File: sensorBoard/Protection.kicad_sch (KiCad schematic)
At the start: 7 parts

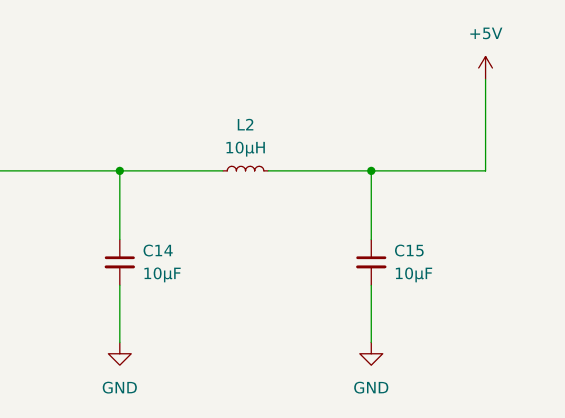
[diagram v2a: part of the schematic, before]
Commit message: started to connect layout. added 0 Ohm resistors to separate the drivers.
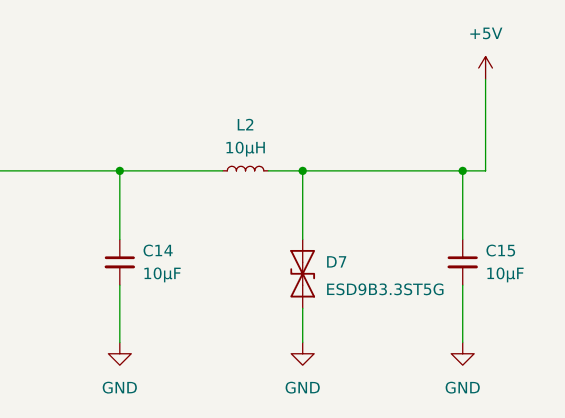
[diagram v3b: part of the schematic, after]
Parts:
- added D7: ESD9B3.3ST5G, Diode_SMD:D_SOD-523, symbol Diode:ESD9B3.3ST5G
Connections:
- net +5V: now also D7.2 (A2)
- net GND: now also D7.1 (A1)
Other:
- moved on the sheet: C15
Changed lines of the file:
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@@
 	)
 	(junction
-		(at 121.92 101.6)
+		(at 114.3 101.6)
+		(diameter 0)
+		(color 0 0 0 0)
+	)
+	(junction
+		(at 132.08 101.6)
 		(diameter 0)
 		(color 0 0 0 0)
@@
 	(wire
 		(pts
-			(xy 121.92 101.6) (xy 134.62 101.6)
-		)
-		(stroke
-			(width 0)
-			(type default)
-		)
-	)
-	(wire
-		(pts
 			(xy 106.68 59.69) (xy 106.68 63.5)
 		)
@@
 	(wire
 		(pts
-			(xy 110.49 101.6) (xy 121.92 101.6)
+			(xy 110.49 101.6) (xy 114.3 101.6)
 		)
 		(stroke
@@
 	(wire
 		(pts
-			(xy 121.92 101.6) (xy 121.92 109.22)
+			(xy 114.3 101.6) (xy 132.08 101.6)
+		)
+		(stroke
+			(width 0)
+			(type default)
+		)
+	)
+	(wire
+		(pts
+			(xy 132.08 101.6) (xy 132.08 109.22)
 		)
 		(stroke
@@
 	(wire
 		(pts
-			(xy 121.92 114.3) (xy 121.92 120.65)
+			(xy 132.08 101.6) (xy 134.62 101.6)
+		)
+		(stroke
+			(width 0)
+			(type default)
+		)
+	)
+	(wire
+		(pts
+			(xy 114.3 116.84) (xy 114.3 120.65)
+		)
+		(stroke
+			(width 0)
+			(type default)
+		)
+	)
+	(wire
+		(pts
+			(xy 132.08 114.3) (xy 132.08 120.65)
 		)
 		(stroke
@@
 		(pts
 			(xy 106.68 50.8) (xy 106.68 52.07)
+		)
+		(stroke
+			(width 0)
+			(type default)
+		)
+	)
+	(wire
+		(pts
+			(xy 114.3 101.6) (xy 114.3 109.22)
 		)
 		(stroke
@@
 	(symbol
 		(lib_id "power:GND")
-		(at 121.92 120.65 0)
+		(at 132.08 120.65 0)
 		(unit 1)
 		(exclude_from_sim no)
@@
 		(fields_autoplaced yes)
 		(property "Reference" "#PWR049"
-			(at 121.92 127 0)
+			(at 132.08 127 0)
 			(effects
 				(font
@@
 		)
 		(property "Value" "GND"
-			(at 121.92 125.73 0)
+			(at 132.08 125.73 0)
 			(effects
 				(font
@@
 		)
 		(property "Footprint" ""
-			(at 121.92 120.65 0)
+			(at 132.08 120.65 0)
 			(effects
 				(font
@@
 		)
 		(property "Datasheet" ""
-			(at 121.92 120.65 0)
+			(at 132.08 120.65 0)
 			(effects
 				(font
@@
 		)
 		(property "Description" "Power symbol creates a global label with name \"GND\" , ground"
-			(at 121.92 120.65 0)
+			(at 132.08 120.65 0)
 			(effects
 				(font
@@
 	(symbol
 		(lib_id "Device:C_Small")
-		(at 121.92 111.76 0)
+		(at 132.08 111.76 0)
 		(unit 1)
 		(exclude_from_sim no)
@@
 		(fields_autoplaced yes)
 		(property "Reference" "C15"
-			(at 124.46 110.4962 0)
+			(at 134.62 110.4962 0)
 			(effects
 				(font
@@
 		)
 		(property "Value" "10µF"
-			(at 124.46 113.0362 0)
+			(at 134.62 113.0362 0)
 			(effects
 				(font
@@
 		)
 		(property "Footprint" "Capacitor_SMD:C_1210_3225Metric"
-			(at 121.92 111.76 0)
+			(at 132.08 111.76 0)
 			(effects
 				(font
@@
 		)
 		(property "Datasheet" "~"
-			(at 121.92 111.76 0)
+			(at 132.08 111.76 0)
 			(effects
 				(font
@@
 		)
 		(property "Description" "Unpolarized capacitor, small symbol"
-			(at 121.92 111.76 0)
+			(at 132.08 111.76 0)
 			(effects
 				(font
@@
 	)
 	(symbol
+		(lib_id "Diode:ESD9B3.3ST5G")
+		(at 114.3 113.03 90)
+		(unit 1)
+		(exclude_from_sim no)
+		(in_bom yes)
+		(on_board yes)
+		(dnp no)
+		(property "Reference" "D7"
+			(at 116.84 111.7599 90)
+			(effects
+				(font
+					(size 1.27 1.27)
+				)
+				(justify right)
+			)
+		)
+		(property "Value" "ESD9B3.3ST5G"
+			(at 116.84 114.808 90)
+			(effects
+				(font
+					(size 1.27 1.27)
+				)
+				(justify right)
+			)
+		)
+		(property "Footprint" "Diode_SMD:D_SOD-523"
+			(at 114.3 113.03 0)
+			(effects
+				(font
+					(size 1.27 1.27)
+				)
+				(hide yes)
+			)
+		)
+		(property "Datasheet" "https://www.mouser.de/ProductDetail/Littelfuse/SMBJ13A?qs=HR2RnyOI4E7jYyaNBU0w0w%3D%3D&srsltid=AfmBOor6_agX3vir1GVOfC2EUzzLngFgs9YFDGWrTlkz9UynbndBGqlu"
+			(at 114.3 113.03 0)
+			(effects
+				(font
+					(size 1.27 1.27)
+				)
+				(hide yes)
+			)
+		)
+		(property "Description" "ESD protection diode, 3.3Vrwm, SOD-923"
+			(at 114.3 113.03 0)
+			(effects
+				(font
+					(size 1.27 1.27)
+				)
+				(hide yes)
+			)
+		)
+		(pin "1"
+		)
+		(pin "2"
+		)
+		(instances
+			(project "sensorBoard"
+				(path "/df1584e9-54f0-49dc-b423-5f64048efa01/eeb71e0f-46bb-44dd-988f-3e7d2427e332"
+					(reference "D7")
+					(unit 1)
+				)
+			)
+		)
+	)
+	(symbol
 		(lib_id "power:GND")
 		(at 127 63.5 0)
@@
 					(unit 1)
 				)
+			)
+		)
+	)
+	(symbol
+		(lib_id "power:GND")
+		(at 114.3 120.65 0)
+		(unit 1)
+		(exclude_from_sim no)
+		(in_bom yes)
+		(on_board yes)
+		(dnp no)
+		(fields_autoplaced yes)
+		(property "Reference" "#PWR083"
+			(at 114.3 127 0)
+			(effects
+				(font
+					(size 1.27 1.27)
+				)
+				(hide yes)
+			)
+		)
+		(property "Value" "GND"
+			(at 114.3 125.73 0)
+			(effects
+				(font
+					(size 1.27 1.27)
+				)
+			)
+		)
+		(property "Footprint" ""
+			(at 114.3 120.65 0)
+			(effects
+				(font
+					(size 1.27 1.27)
+				)
+				(hide yes)
+			)
+		)
+		(property "Datasheet" ""
+			(at 114.3 120.65 0)
+			(effects
+				(font
+					(size 1.27 1.27)
+				)
+				(hide yes)
+			)
+		)
+		(property "Description" "Power symbol creates a global label with name \"GND\" , ground"
+			(at 114.3 120.65 0)
+			(effects
+				(font
+					(size 1.27 1.27)
+				)
+				(hide yes)
+			)
+		)
+		(pin "1"
+		)
+		(instances
+			(project "sensorBoard"
+				(path "/df1584e9-54f0-49dc-b423-5f64048efa01/eeb71e0f-46bb-44dd-988f-3e7d2427e332"
+					(reference "#PWR083")
+					(unit 1)
+				)

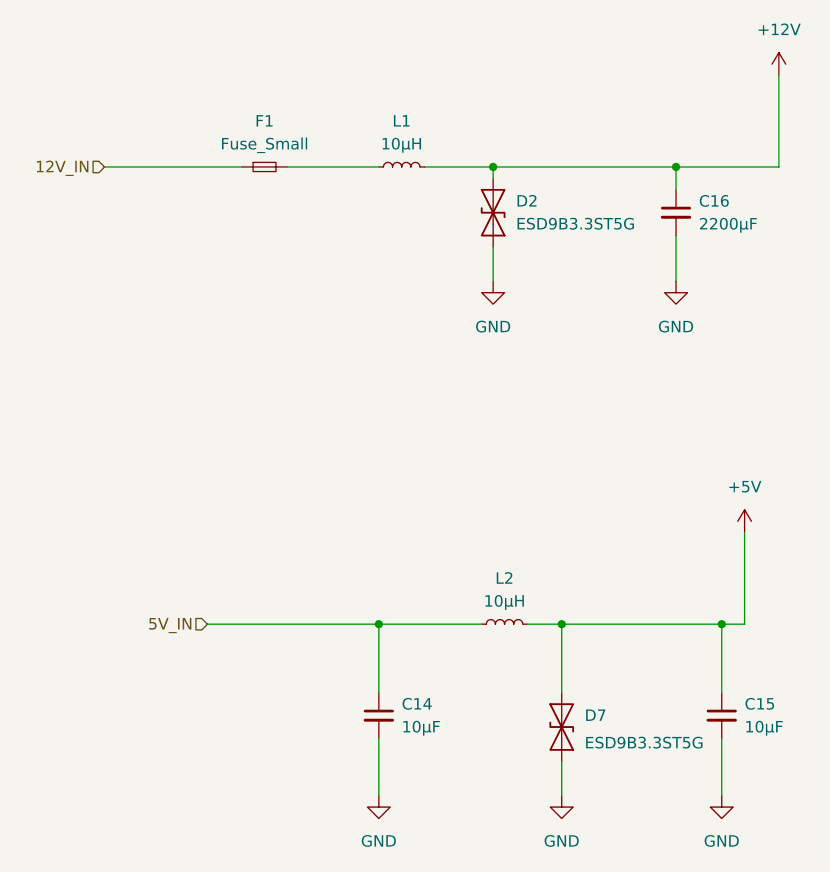
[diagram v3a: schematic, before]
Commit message: new two separate pcbs
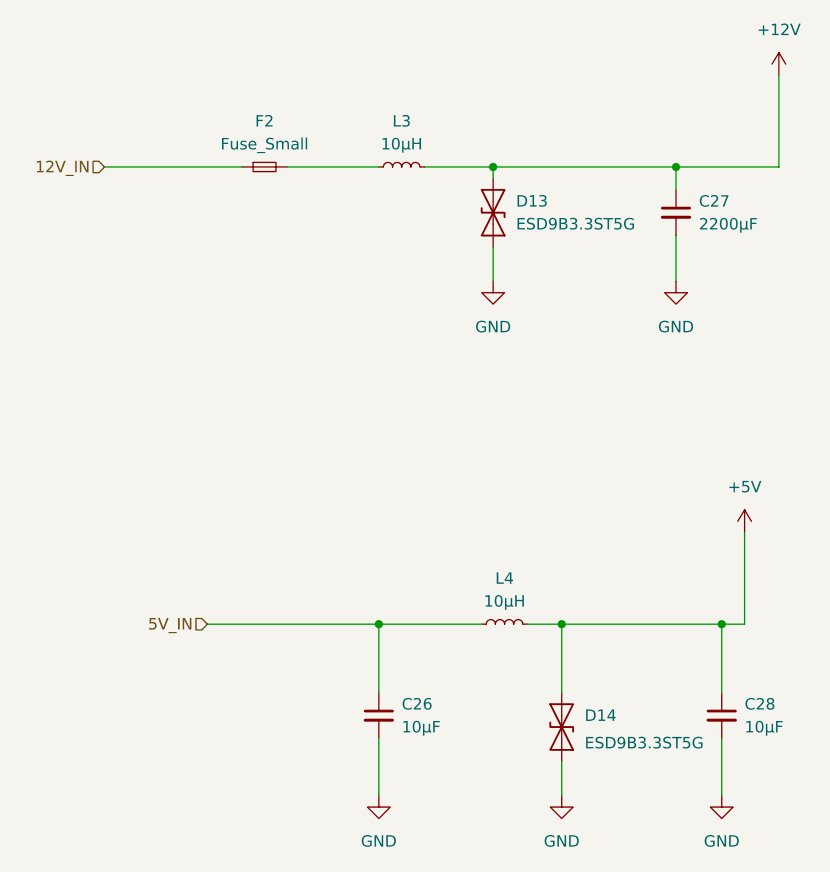
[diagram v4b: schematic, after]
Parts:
- renumbered C14 to C26, C16 to C27, C15 to C28, D2 to D13, D7 to D14, F1 to F2, L1 to L3, L2 to L4
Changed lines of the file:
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@@
 		(dnp no)
 		(fields_autoplaced yes)
-		(property "Reference" "L2"
+		(property "Reference" "L4"
 			(at 107.95 96.52 90)
 			(effects
@@
 		(instances
 			(project "sensorBoard"
-				(path "/df1584e9-54f0-49dc-b423-5f64048efa01/eeb71e0f-46bb-44dd-988f-3e7d2427e332"
-					(reference "L2")
+				(path "/df1584e9-54f0-49dc-b423-5f64048efa01/60fa4213-9bcb-42a7-994a-420953d9bcb7/85dfac51-e25c-4ad4-a068-3d93efddec4c"
+					(reference "L6")
+					(unit 1)
+				)
+				(path "/df1584e9-54f0-49dc-b423-5f64048efa01/99847452-c15f-478e-a49b-00c0f2bcd04b/3442ede8-ab67-47a2-877b-54a427eb9a90"
+					(reference "L4")
 					(unit 1)
 				)
@@
 		(dnp no)
 		(fields_autoplaced yes)
-		(property "Reference" "#PWR049"
+		(property "Reference" "#PWR0128"
 			(at 132.08 127 0)
 			(effects
@@
 		(instances
 			(project "sensorBoard"
-				(path "/df1584e9-54f0-49dc-b423-5f64048efa01/eeb71e0f-46bb-44dd-988f-3e7d2427e332"
-					(reference "#PWR049")
+				(path "/df1584e9-54f0-49dc-b423-5f64048efa01/60fa4213-9bcb-42a7-994a-420953d9bcb7/85dfac51-e25c-4ad4-a068-3d93efddec4c"
+					(reference "#PWR0210")
+					(unit 1)
+				)
+				(path "/df1584e9-54f0-49dc-b423-5f64048efa01/99847452-c15f-478e-a49b-00c0f2bcd04b/3442ede8-ab67-47a2-877b-54a427eb9a90"
+					(reference "#PWR0128")
 					(unit 1)
 				)
@@
 		(dnp no)
 		(fields_autoplaced yes)
-		(property "Reference" "C15"
+		(property "Reference" "C28"
 			(at 134.62 110.4962 0)
 			(effects
@@
 		(instances
 			(project "sensorBoard"
-				(path "/df1584e9-54f0-49dc-b423-5f64048efa01/eeb71e0f-46bb-44dd-988f-3e7d2427e332"
-					(reference "C15")
+				(path "/df1584e9-54f0-49dc-b423-5f64048efa01/60fa4213-9bcb-42a7-994a-420953d9bcb7/85dfac51-e25c-4ad4-a068-3d93efddec4c"
+					(reference "C45")
+					(unit 1)
+				)
+				(path "/df1584e9-54f0-49dc-b423-5f64048efa01/99847452-c15f-478e-a49b-00c0f2bcd04b/3442ede8-ab67-47a2-877b-54a427eb9a90"
+					(reference "C28")
 					(unit 1)
 				)
@@
 		(dnp no)
 		(fields_autoplaced yes)
-		(property "Reference" "#PWR045"
+		(property "Reference" "#PWR0130"
 			(at 138.43 44.45 0)
 			(effects
@@
 		)
 		(instances
-			(project ""
-				(path "/df1584e9-54f0-49dc-b423-5f64048efa01/eeb71e0f-46bb-44dd-988f-3e7d2427e332"
-					(reference "#PWR045")
+			(project "sensorBoard"
+				(path "/df1584e9-54f0-49dc-b423-5f64048efa01/60fa4213-9bcb-42a7-994a-420953d9bcb7/85dfac51-e25c-4ad4-a068-3d93efddec4c"
+					(reference "#PWR0212")
+					(unit 1)
+				)
+				(path "/df1584e9-54f0-49dc-b423-5f64048efa01/99847452-c15f-478e-a49b-00c0f2bcd04b/3442ede8-ab67-47a2-877b-54a427eb9a90"
+					(reference "#PWR0130")
 					(unit 1)
 				)
@@
 		(on_board yes)
 		(dnp no)
-		(property "Reference" "D7"
+		(property "Reference" "D14"
 			(at 116.84 111.7599 90)
 			(effects
@@
 		(instances
 			(project "sensorBoard"
-				(path "/df1584e9-54f0-49dc-b423-5f64048efa01/eeb71e0f-46bb-44dd-988f-3e7d2427e332"
-					(reference "D7")
+				(path "/df1584e9-54f0-49dc-b423-5f64048efa01/60fa4213-9bcb-42a7-994a-420953d9bcb7/85dfac51-e25c-4ad4-a068-3d93efddec4c"
+					(reference "D21")
+					(unit 1)
+				)
+				(path "/df1584e9-54f0-49dc-b423-5f64048efa01/99847452-c15f-478e-a49b-00c0f2bcd04b/3442ede8-ab67-47a2-877b-54a427eb9a90"
+					(reference "D14")
 					(unit 1)
 				)
@@
 		(dnp no)
 		(fields_autoplaced yes)
-		(property "Reference" "#PWR050"
+		(property "Reference" "#PWR0127"
 			(at 127 69.85 0)
 			(effects
@@
 		)
 		(instances
-			(project ""
-				(path "/df1584e9-54f0-49dc-b423-5f64048efa01/eeb71e0f-46bb-44dd-988f-3e7d2427e332"
-					(reference "#PWR050")
+			(project "sensorBoard"
+				(path "/df1584e9-54f0-49dc-b423-5f64048efa01/60fa4213-9bcb-42a7-994a-420953d9bcb7/85dfac51-e25c-4ad4-a068-3d93efddec4c"
+					(reference "#PWR0209")
+					(unit 1)
+				)
+				(path "/df1584e9-54f0-49dc-b423-5f64048efa01/99847452-c15f-478e-a49b-00c0f2bcd04b/3442ede8-ab67-47a2-877b-54a427eb9a90"
+					(reference "#PWR0127")
 					(unit 1)
 				)
@@
 		(dnp no)
 		(fields_autoplaced yes)
-		(property "Reference" "L1"
+		(property "Reference" "L3"
 			(at 96.52 45.72 90)
 			(effects
@@
 		)
 		(instances
-			(project ""
-				(path "/df1584e9-54f0-49dc-b423-5f64048efa01/eeb71e0f-46bb-44dd-988f-3e7d2427e332"
-					(reference "L1")
+			(project "sensorBoard"
+				(path "/df1584e9-54f0-49dc-b423-5f64048efa01/60fa4213-9bcb-42a7-994a-420953d9bcb7/85dfac51-e25c-4ad4-a068-3d93efddec4c"
+					(reference "L5")
+					(unit 1)
+				)
+				(path "/df1584e9-54f0-49dc-b423-5f64048efa01/99847452-c15f-478e-a49b-00c0f2bcd04b/3442ede8-ab67-47a2-877b-54a427eb9a90"
+					(reference "L3")
 					(unit 1)
 				)
@@
 		(dnp no)
 		(fields_autoplaced yes)
-		(property "Reference" "#PWR048"
+		(property "Reference" "#PWR0124"
 			(at 93.98 127 0)
 			(effects
@@
 		)
 		(instances
-			(project ""
-				(path "/df1584e9-54f0-49dc-b423-5f64048efa01/eeb71e0f-46bb-44dd-988f-3e7d2427e332"
-					(reference "#PWR048")
+			(project "sensorBoard"
+				(path "/df1584e9-54f0-49dc-b423-5f64048efa01/60fa4213-9bcb-42a7-994a-420953d9bcb7/85dfac51-e25c-4ad4-a068-3d93efddec4c"
+					(reference "#PWR0206")
+					(unit 1)
+				)
+				(path "/df1584e9-54f0-49dc-b423-5f64048efa01/99847452-c15f-478e-a49b-00c0f2bcd04b/3442ede8-ab67-47a2-877b-54a427eb9a90"
+					(reference "#PWR0124")
 					(unit 1)
 				)
@@
 		(dnp no)
 		(fields_autoplaced yes)
-		(property "Reference" "D2"
+		(property "Reference" "D13"
 			(at 109.22 54.6099 90)
 			(effects
@@
 		)
 		(instances
-			(project ""
-				(path "/df1584e9-54f0-49dc-b423-5f64048efa01/eeb71e0f-46bb-44dd-988f-3e7d2427e332"
-					(reference "D2")
+			(project "sensorBoard"
+				(path "/df1584e9-54f0-49dc-b423-5f64048efa01/60fa4213-9bcb-42a7-994a-420953d9bcb7/85dfac51-e25c-4ad4-a068-3d93efddec4c"
+					(reference "D20")
+					(unit 1)
+				)
+				(path "/df1584e9-54f0-49dc-b423-5f64048efa01/99847452-c15f-478e-a49b-00c0f2bcd04b/3442ede8-ab67-47a2-877b-54a427eb9a90"
+					(reference "D13")
 					(unit 1)
 				)
@@
 		(dnp no)
 		(fields_autoplaced yes)
-		(property "Reference" "#PWR083"
+		(property "Reference" "#PWR0126"
 			(at 114.3 127 0)
 			(effects
@@
 		(instances
 			(project "sensorBoard"
-				(path "/df1584e9-54f0-49dc-b423-5f64048efa01/eeb71e0f-46bb-44dd-988f-3e7d2427e332"
-					(reference "#PWR083")
+				(path "/df1584e9-54f0-49dc-b423-5f64048efa01/60fa4213-9bcb-42a7-994a-420953d9bcb7/85dfac51-e25c-4ad4-a068-3d93efddec4c"
+					(reference "#PWR0208")
+					(unit 1)
+				)
+				(path "/df1584e9-54f0-49dc-b423-5f64048efa01/99847452-c15f-478e-a49b-00c0f2bcd04b/3442ede8-ab67-47a2-877b-54a427eb9a90"
+					(reference "#PWR0126")
 					(unit 1)
 				)
@@
 		(dnp no)
 		(fields_autoplaced yes)
-		(property "Reference" "#PWR043"
+		(property "Reference" "#PWR0125"
 			(at 106.68 69.85 0)
 			(effects
@@
 		)
 		(instances
-			(project ""
-				(path "/df1584e9-54f0-49dc-b423-5f64048efa01/eeb71e0f-46bb-44dd-988f-3e7d2427e332"
-					(reference "#PWR043")
+			(project "sensorBoard"
+				(path "/df1584e9-54f0-49dc-b423-5f64048efa01/60fa4213-9bcb-42a7-994a-420953d9bcb7/85dfac51-e25c-4ad4-a068-3d93efddec4c"
+					(reference "#PWR0207")
+					(unit 1)
+				)
+				(path "/df1584e9-54f0-49dc-b423-5f64048efa01/99847452-c15f-478e-a49b-00c0f2bcd04b/3442ede8-ab67-47a2-877b-54a427eb9a90"
+					(reference "#PWR0125")
 					(unit 1)
 				)
@@
 		(dnp no)
 		(fields_autoplaced yes)
-		(property "Reference" "C14"
+		(property "Reference" "C26"
 			(at 96.52 110.4962 0)
 			(effects
@@
 		)
 		(instances
-			(project ""
-				(path "/df1584e9-54f0-49dc-b423-5f64048efa01/eeb71e0f-46bb-44dd-988f-3e7d2427e332"
-					(reference "C14")
+			(project "sensorBoard"
+				(path "/df1584e9-54f0-49dc-b423-5f64048efa01/60fa4213-9bcb-42a7-994a-420953d9bcb7/85dfac51-e25c-4ad4-a068-3d93efddec4c"
+					(reference "C43")
+					(unit 1)
+				)
+				(path "/df1584e9-54f0-49dc-b423-5f64048efa01/99847452-c15f-478e-a49b-00c0f2bcd04b/3442ede8-ab67-47a2-877b-54a427eb9a90"
+					(reference "C26")
 					(unit 1)
 				)
@@
 		(dnp no)
 		(fields_autoplaced yes)
-		(property "Reference" "#PWR047"
+		(property "Reference" "#PWR0129"
 			(at 134.62 95.25 0)
 			(effects
@@
 		)
 		(instances
-			(project ""
-				(path "/df1584e9-54f0-49dc-b423-5f64048efa01/eeb71e0f-46bb-44dd-988f-3e7d2427e332"
-					(reference "#PWR047")
+			(project "sensorBoard"
+				(path "/df1584e9-54f0-49dc-b423-5f64048efa01/60fa4213-9bcb-42a7-994a-420953d9bcb7/85dfac51-e25c-4ad4-a068-3d93efddec4c"
+					(reference "#PWR0211")
+					(unit 1)
+				)
+				(path "/df1584e9-54f0-49dc-b423-5f64048efa01/99847452-c15f-478e-a49b-00c0f2bcd04b/3442ede8-ab67-47a2-877b-54a427eb9a90"
+					(reference "#PWR0129")
 					(unit 1)
 				)
@@
 		(dnp no)
 		(fields_autoplaced yes)
-		(property "Reference" "C16"
+		(property "Reference" "C27"
 			(at 129.54 54.6162 0)
 			(effects
@@
 		(instances
 			(project "sensorBoard"
-				(path "/df1584e9-54f0-49dc-b423-5f64048efa01/eeb71e0f-46bb-44dd-988f-3e7d2427e332"
-					(reference "C16")
+				(path "/df1584e9-54f0-49dc-b423-5f64048efa01/60fa4213-9bcb-42a7-994a-420953d9bcb7/85dfac51-e25c-4ad4-a068-3d93efddec4c"
+					(reference "C44")
+					(unit 1)
+				)
+				(path "/df1584e9-54f0-49dc-b423-5f64048efa01/99847452-c15f-478e-a49b-00c0f2bcd04b/3442ede8-ab67-47a2-877b-54a427eb9a90"
+					(reference "C27")
 					(unit 1)
 				)
@@
 		(dnp no)
 		(fields_autoplaced yes)
-		(property "Reference" "F1"
+		(property "Reference" "F2"
 			(at 81.28 45.72 0)
 			(effects
@@
 		)
 		(instances
-			(project ""
-				(path "/df1584e9-54f0-49dc-b423-5f64048efa01/eeb71e0f-46bb-44dd-988f-3e7d2427e332"
-					(reference "F1")
-					(unit 1)
-				)
+			(project "sensorBoard"
+				(path "/df1584e9-54f0-49dc-b423-5f64048efa01/60fa4213-9bcb-42a7-994a-420953d9bcb7/85dfac51-e25c-4ad4-a068-3d93efddec4c"
+					(reference "F3")
+					(unit 1)
+				)
+				(path "/df1584e9-54f0-49dc-b423-5f64048efa01/99847452-c15f-478e-a49b-00c0f2bcd04b/3442ede8-ab67-47a2-877b-54a427eb9a90"
+					(reference "F2")
+					(unit 1)
+				)
